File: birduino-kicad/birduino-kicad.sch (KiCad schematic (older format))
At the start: 29 parts, among them J1 Conn_01x03_Male, J10 Conn_01x01_Male, J11 Conn_01x01_Male, J2 Conn_01x02_Male, J3 Conn_02x05_Odd_Even, J4 Conn_01x04, J5 Conn_01x01_Male, J6 Conn_01x01_Male, J7 Conn_01x01_Male, J8 Conn_02x02_Odd_Even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

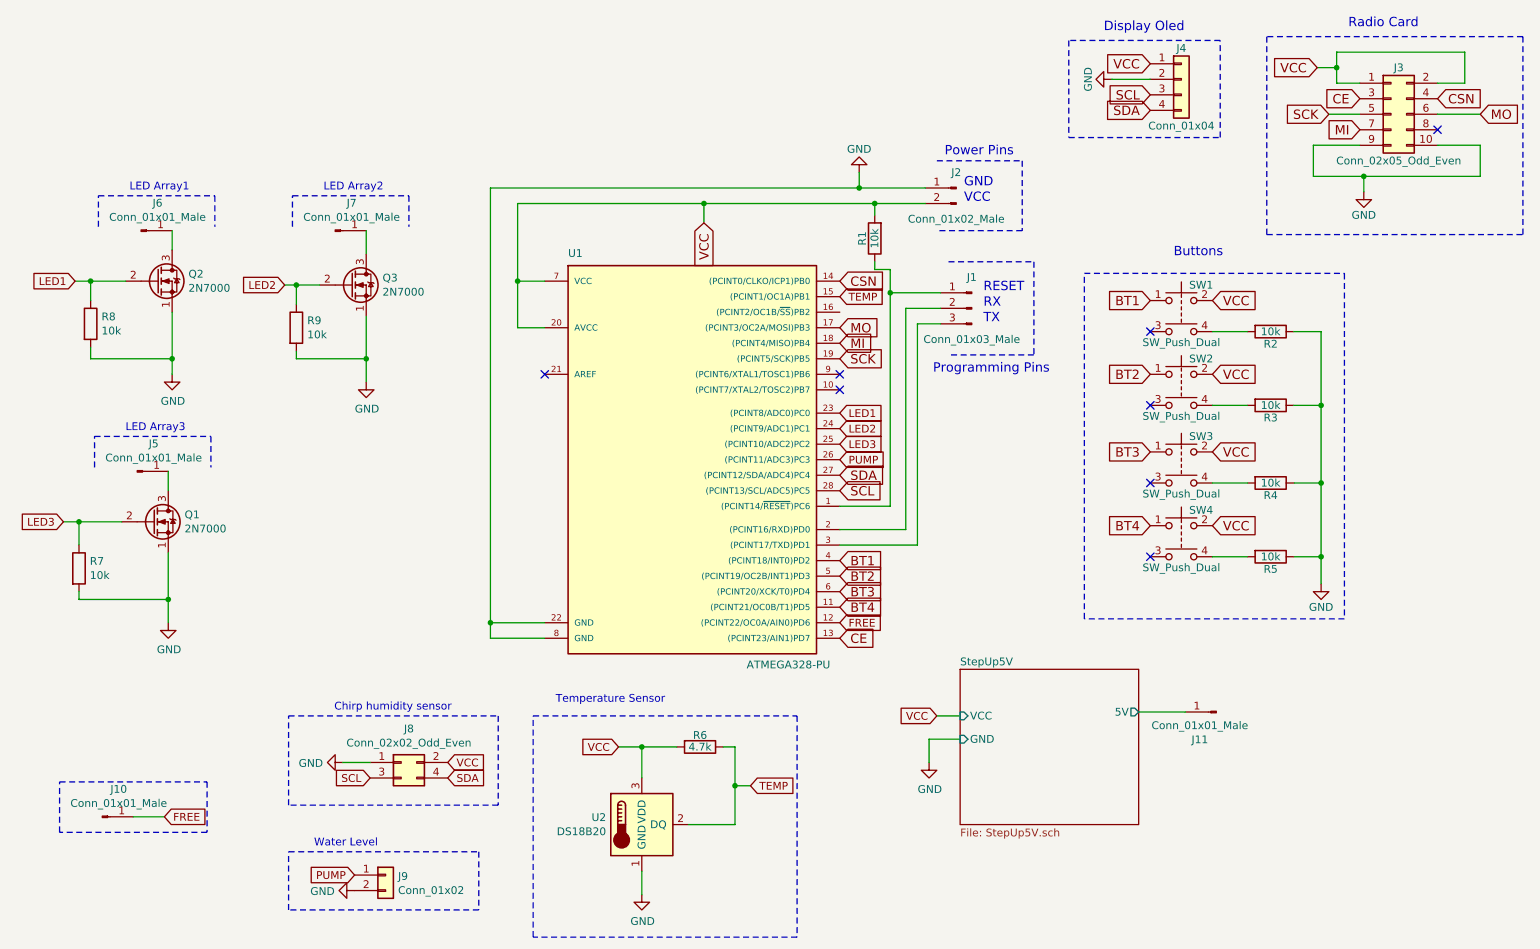
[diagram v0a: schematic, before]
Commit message: feat: added Crytal to PCB. Added new images to readme.
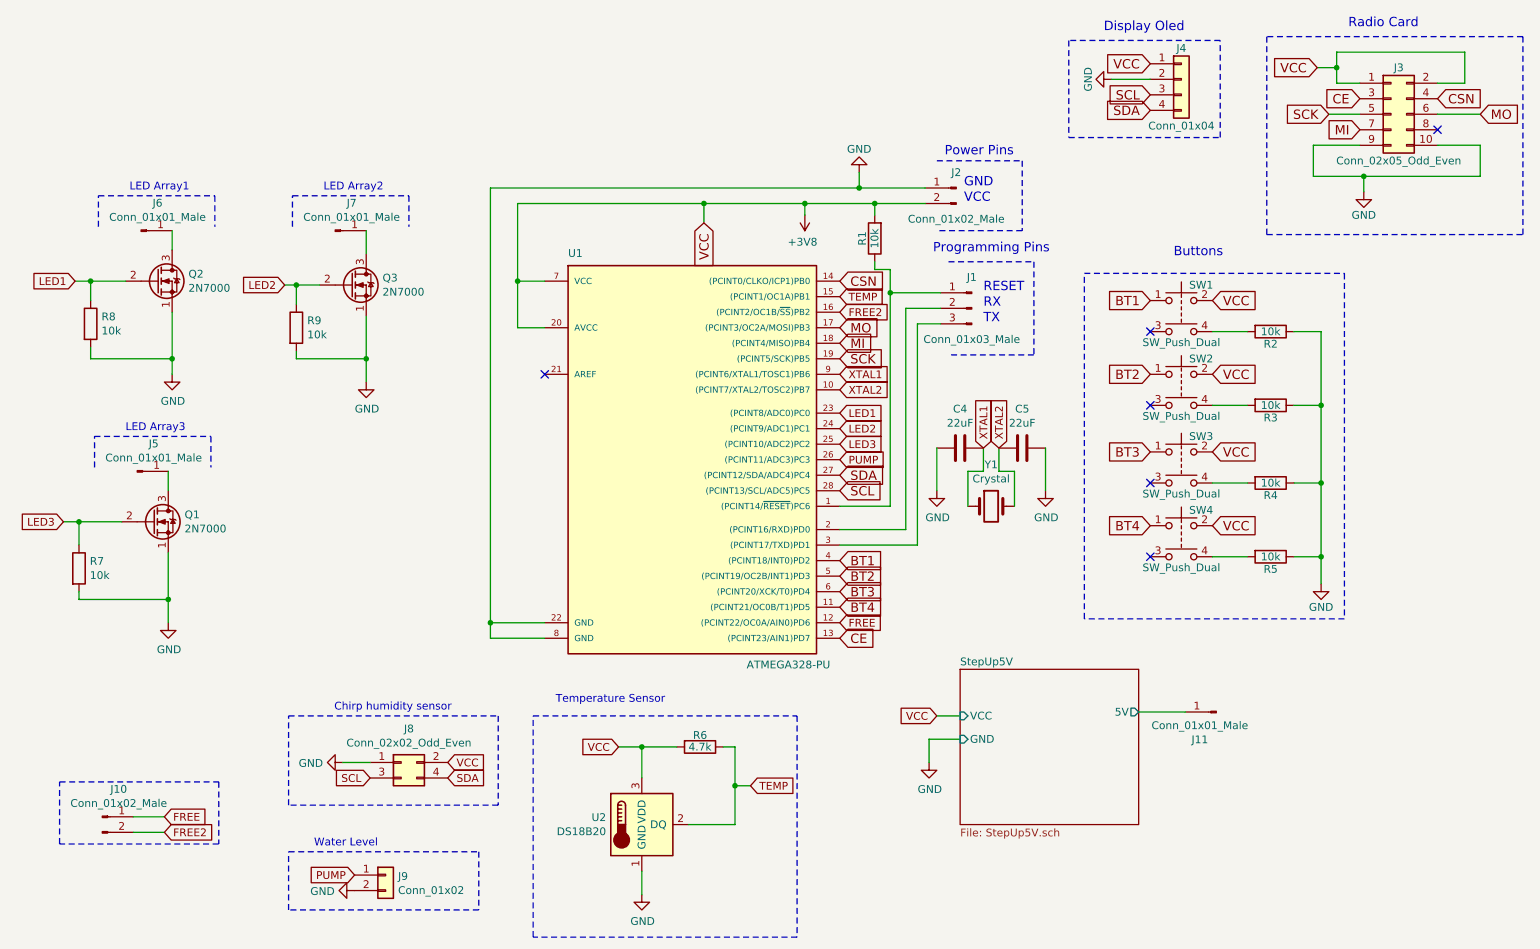
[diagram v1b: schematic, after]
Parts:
- removed J10: Conn_01x01_Male, Connector_PinHeader_2.54mm:PinHeader_1x01_P2.54mm_Vertical, symbol Connector:Conn_01x01_Male
- added C4, C5: 22uF, Capacitor_THT:C_Disc_D6.0mm_W2.5mm_P5.00mm, symbol Device:C
- added J10: Conn_01x02_Male, Connector_PinHeader_2.54mm:PinHeader_1x02_P2.54mm_Vertical, symbol birduino-kicad-rescue:Conn_01x02_Male
- added Y1: Crystal, Crystal:Crystal_HC49-4H_Vertical, symbol Device:Crystal
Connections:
- net FREE: now also J10.1 (Pin_1)
- net GND: now also C4.2, C5.1
- net XTAL2: now reaches U1.10 ((PCINT7/XTAL2/TOSC2)PB7)
- net XTAL2: now also C5.2, Y1.2
- net FREE2: now reaches U1.16 ((PCINT2/OC1B/~SS~)PB2)
- net FREE2: now also J10.2 (Pin_2)
- net XTAL1: now reaches U1.9 ((PCINT6/XTAL1/TOSC1)PB6)
- net XTAL1: now also C4.1, Y1.1
- net VCC renamed +3V8
- no-connect marks 8 -> 6
